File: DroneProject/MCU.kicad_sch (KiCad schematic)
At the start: 24 parts, among them U41 STM32F410RBT6, Y41 LFXTAL003151

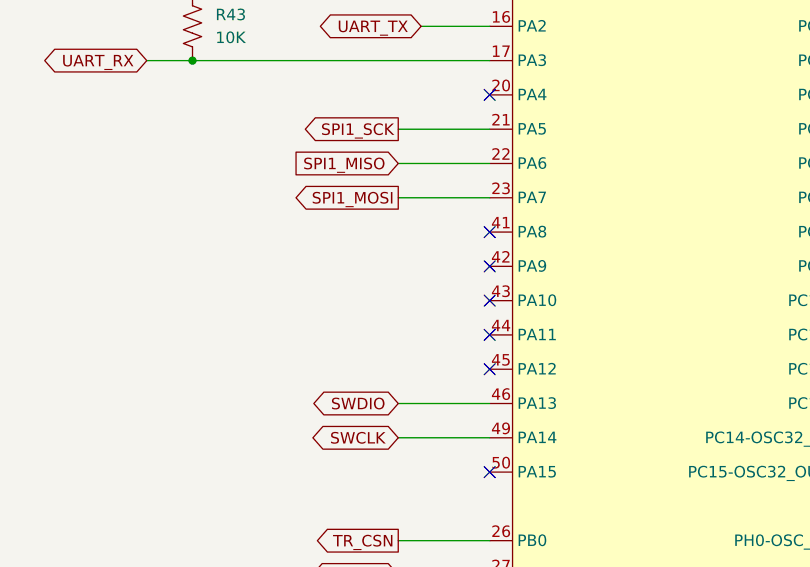
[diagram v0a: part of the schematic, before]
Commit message: Added mounting holes and some more testpoints.  Also started on PCB with dimesions and mounting holes measured and placed
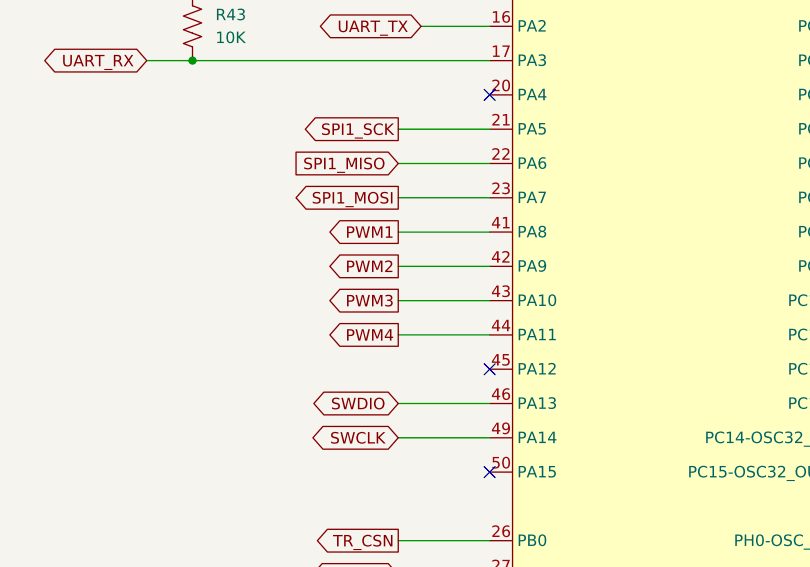
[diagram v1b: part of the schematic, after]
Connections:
- net PWM1: now reaches U41.41 (PA8)
- net PWM2: now reaches U41.42 (PA9)
- net PWM3: now reaches U41.43 (PA10)
- net PWM4: now reaches U41.44 (PA11)
- no-connect marks 23 -> 19
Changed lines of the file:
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@@
-	)
-	(no_connect
-		(at 68.58 71.12)
 	)
 	(no_connect
@@
 	)
 	(no_connect
-		(at 68.58 78.74)
-	)
-	(no_connect
 		(at 68.58 132.08)
 	)
 	(no_connect
-		(at 68.58 82.55)
-	)
-	(no_connect
 		(at 68.58 44.45)
 	)
@@
 	)
 	(no_connect
-		(at 68.58 74.93)
-	)
-	(no_connect
 		(at 109.22 52.07)
 	)
@@
 	(wire
 		(pts
+			(xy 58.42 71.12) (xy 68.58 71.12)
+		)
+		(stroke
+			(width 0)
+			(type default)
+		)
+	)
+	(wire
+		(pts
 			(xy 170.18 45.72) (xy 166.37 45.72)
 		)
@@
 	(wire
 		(pts
+			(xy 58.42 82.55) (xy 68.58 82.55)
+		)
+		(stroke
+			(width 0)
+			(type default)
+		)
+	)
+	(wire
+		(pts
 			(xy 166.37 45.72) (xy 166.37 48.26)
 		)
@@
 	(wire
 		(pts
+			(xy 58.42 74.93) (xy 68.58 74.93)
+		)
+		(stroke
+			(width 0)
+			(type default)
+		)
+	)
+	(wire
+		(pts
 			(xy 207.01 43.18) (xy 207.01 45.72)
 		)
@@
 		(pts
 			(xy 274.32 25.4) (xy 261.62 25.4)
+		)
+		(stroke
+			(width 0)
+			(type default)
+		)
+	)
+	(wire
+		(pts
+			(xy 58.42 78.74) (xy 68.58 78.74)
 		)
 		(stroke
@@
 		)
 	)
+	(global_label "PWM4"
+		(shape output)
+		(at 58.42 82.55 180)
+		(fields_autoplaced yes)
+		(effects
+			(font
+				(size 1.27 1.27)
+			)
+			(justify right)
+		)
+		(property "Intersheetrefs" "${INTERSHEET_REFS}"
+			(at 50.0525 82.55 0)
+			(effects
+				(font
+					(size 1.27 1.27)
+				)
+				(justify right)
+			)
+		)
+	)
 	(global_label "SPI1_MISO"
 		(shape input)
@@
 		)
 	)
+	(global_label "PWM1"
+		(shape output)
+		(at 58.42 71.12 180)
+		(fields_autoplaced yes)
+		(effects
+			(font
+				(size 1.27 1.27)
+			)
+			(justify right)
+		)
+		(property "Intersheetrefs" "${INTERSHEET_REFS}"
+			(at 50.0525 71.12 0)
+			(effects
+				(font
+					(size 1.27 1.27)
+				)
+				(justify right)
+			)
+		)
+	)
 	(global_label "SWCLK"
 		(shape bidirectional)
@@
 			)
 		)
+	)
+	(global_label "PWM3"
+		(shape output)
+		(at 58.42 78.74 180)
+		(fields_autoplaced yes)
+		(effects
+			(font
+				(size 1.27 1.27)
+			)
+			(justify right)
+		)
+		(property "Intersheetrefs" "${INTERSHEET_REFS}"
+			(at 50.0525 78.74 0)
+			(effects
+				(font
+					(size 1.27 1.27)
+				)
+				(justify right)
+			)
+		)
+	)
+	(global_label "PWM2"
+		(shape output)
+		(at 58.42 74.93 180)
+		(fields_autoplaced yes)
+		(effects
+			(font
+				(size 1.27 1.27)
+			)
+			(justify right)
+		)
+		(property "Intersheetrefs" "${INTERSHEET_REFS}"
+			(at 50.0525 74.93 0)
+			(effects
+				(font
+					(size 1.27 1.27)
+				)
+				(justify right)
+			)
+		)

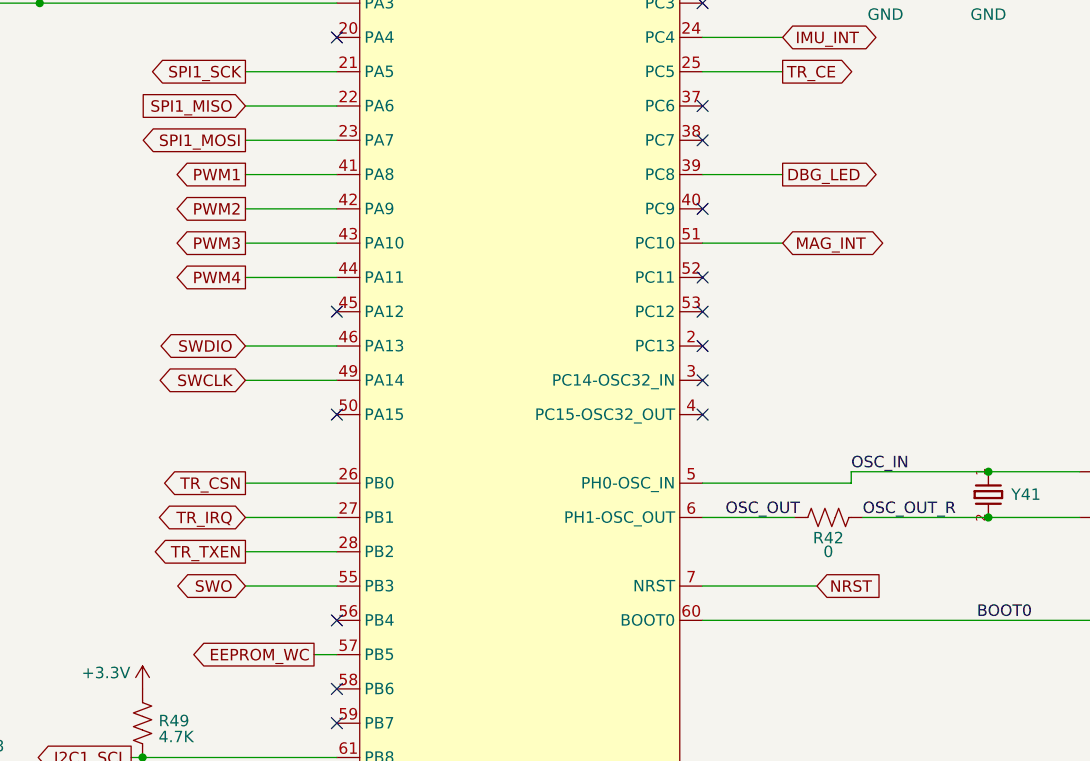
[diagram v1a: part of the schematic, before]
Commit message: Added a second MCU for motor control.  Removed 5V rail.  Added COM switching for SWD and UART external headers
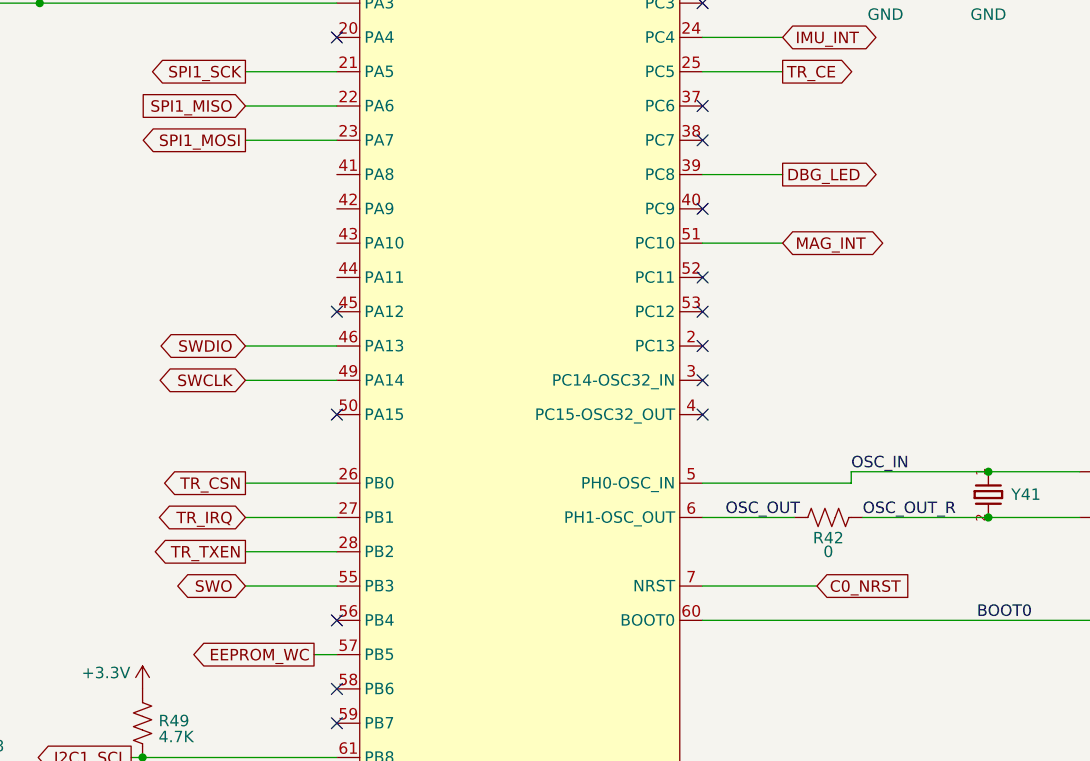
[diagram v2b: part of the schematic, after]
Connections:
- net NRST renamed C0_NRST
- net PWM1: no longer names the net of U41.41 (PA8)
- net PWM2: no longer names the net of U41.42 (PA9)
- net PWM3: no longer names the net of U41.43 (PA10)
- net PWM4: no longer names the net of U41.44 (PA11)
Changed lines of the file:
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@@
-	(wire
-		(pts
-			(xy 58.42 71.12) (xy 68.58 71.12)
-		)
-		(stroke
-			(width 0)
-			(type default)
-		)
-	)
 	(wire
 		(pts
@@
 	(wire
 		(pts
-			(xy 58.42 82.55) (xy 68.58 82.55)
-		)
-		(stroke
-			(width 0)
-			(type default)
-		)
-	)
-	(wire
-		(pts
 			(xy 166.37 45.72) (xy 166.37 48.26)
 		)
@@
 	(wire
 		(pts
-			(xy 58.42 74.93) (xy 68.58 74.93)
-		)
-		(stroke
-			(width 0)
-			(type default)
-		)
-	)
-	(wire
-		(pts
 			(xy 207.01 43.18) (xy 207.01 45.72)
 		)
@@
 		(pts
 			(xy 274.32 25.4) (xy 261.62 25.4)
-		)
-		(stroke
-			(width 0)
-			(type default)
-		)
-	)
-	(wire
-		(pts
-			(xy 58.42 78.74) (xy 68.58 78.74)
 		)
 		(stroke
@@
 		)
 	)
-	(global_label "PWM4"
-		(shape output)
-		(at 58.42 82.55 180)
-		(fields_autoplaced yes)
-		(effects
-			(font
-				(size 1.27 1.27)
-			)
-			(justify right)
-		)
-		(property "Intersheetrefs" "${INTERSHEET_REFS}"
-			(at 50.0525 82.55 0)
-			(effects
-				(font
-					(size 1.27 1.27)
-				)
-				(justify right)
-			)
-		)
-	)
 	(global_label "SPI1_MISO"
 		(shape input)
@@
 		)
 	)
-	(global_label "PWM1"
-		(shape output)
-		(at 58.42 71.12 180)
-		(fields_autoplaced yes)
-		(effects
-			(font
-				(size 1.27 1.27)
-			)
-			(justify right)
-		)
-		(property "Intersheetrefs" "${INTERSHEET_REFS}"
-			(at 50.0525 71.12 0)
-			(effects
-				(font
-					(size 1.27 1.27)
-				)
-				(justify right)
-			)
-		)
-	)
 	(global_label "SWCLK"
 		(shape bidirectional)
@@
 		)
 	)
-	(global_label "PWM3"
-		(shape output)
-		(at 58.42 78.74 180)
-		(fields_autoplaced yes)
-		(effects
-			(font
-				(size 1.27 1.27)
-			)
-			(justify right)
-		)
-		(property "Intersheetrefs" "${INTERSHEET_REFS}"
-			(at 50.0525 78.74 0)
-			(effects
-				(font
-					(size 1.27 1.27)
-				)
-				(justify right)
-			)
-		)
-	)
-	(global_label "PWM2"
-		(shape output)
-		(at 58.42 74.93 180)
-		(fields_autoplaced yes)
-		(effects
-			(font
-				(size 1.27 1.27)
-			)
-			(justify right)
-		)
-		(property "Intersheetrefs" "${INTERSHEET_REFS}"
-			(at 50.0525 74.93 0)
-			(effects
-				(font
-					(size 1.27 1.27)
-				)
-				(justify right)
-			)
-		)
-	)
 	(global_label "TR_TXEN"
 		(shape output)
@@
 		)
 	)
-	(global_label "NRST"
+	(global_label "C0_NRST"
 		(shape input)
 		(at 121.92 116.84 0)
@@
 		)
 		(property "Intersheetrefs" "${INTERSHEET_REFS}"
-			(at 129.6828 116.84 0)
-			(effects
-				(font
+			(at 133.1299 116.84 0)
+			(effects
+				(font

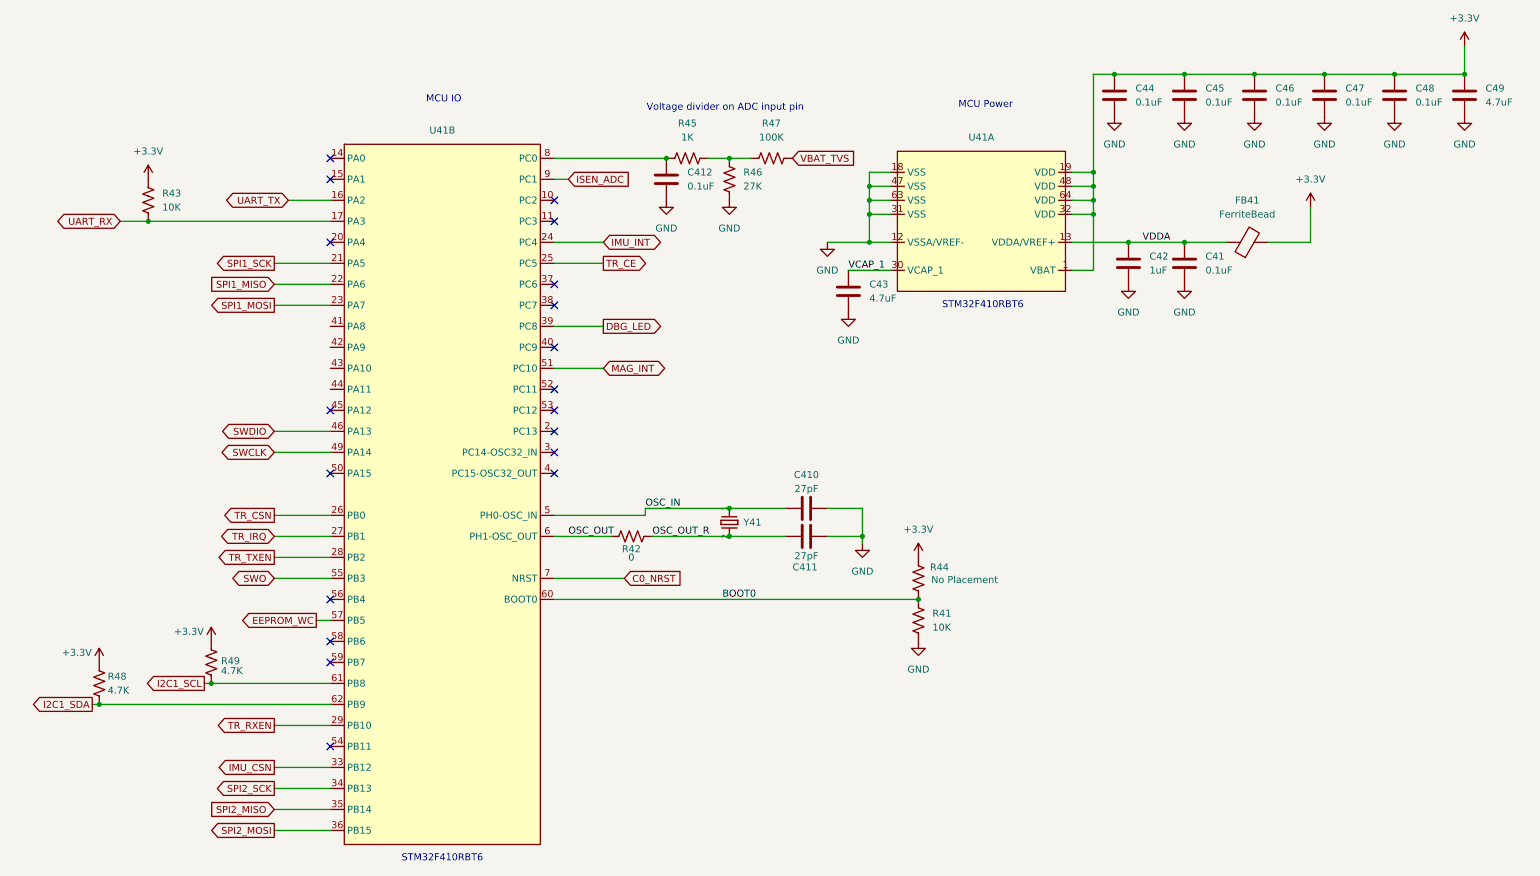
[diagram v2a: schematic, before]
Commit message: Changed motor controller to higher pin count MCU.  Defined all the pins for 3x PWM control over 4 motors.  Renamed a couple of global IO signals to indicate MCU origin (C0 vs C1)
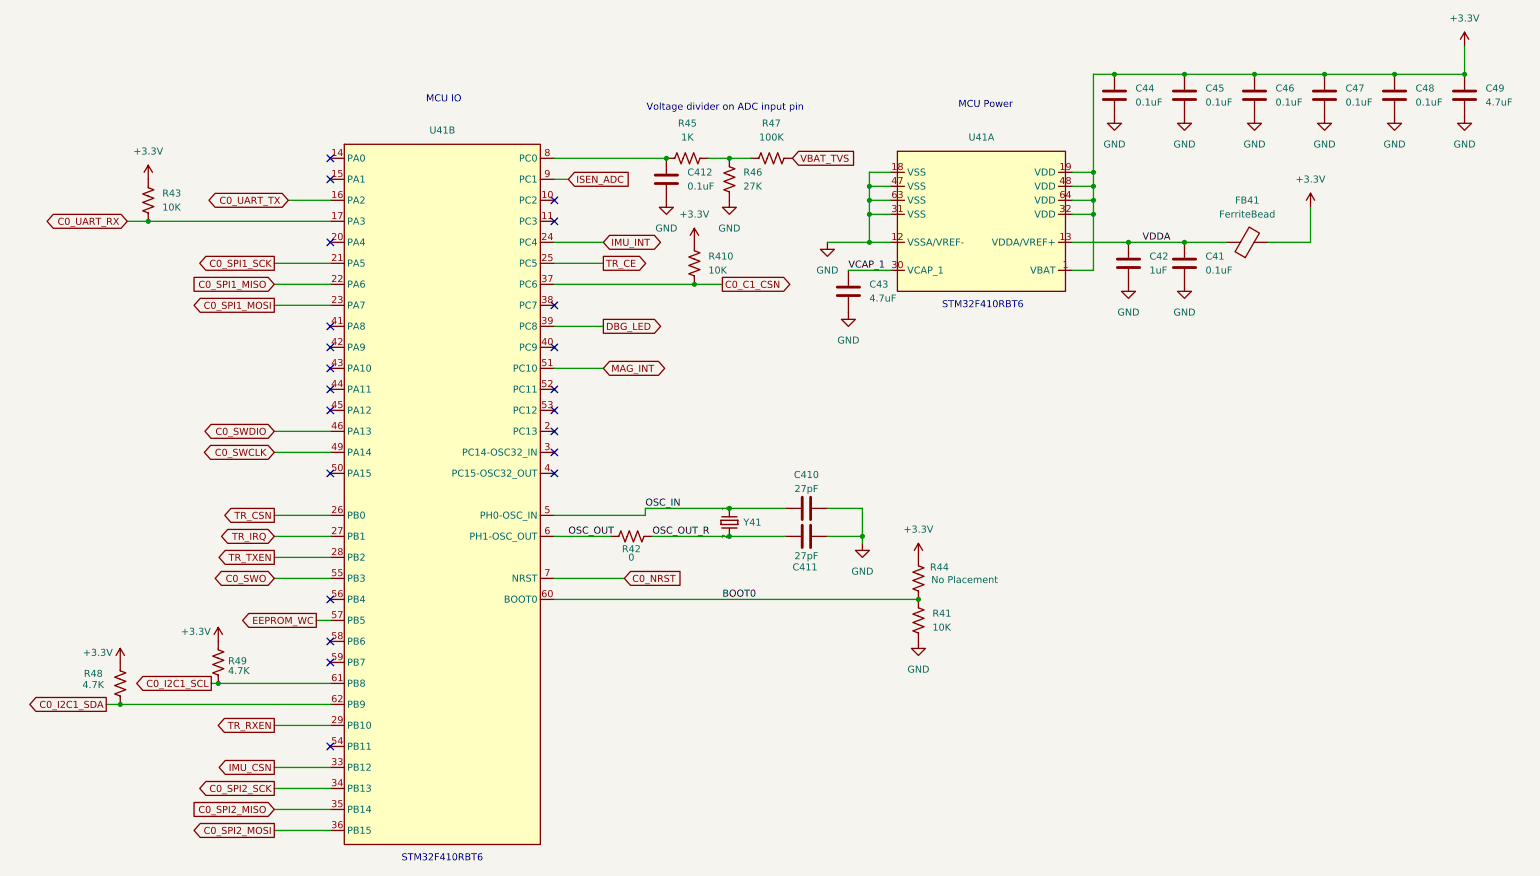
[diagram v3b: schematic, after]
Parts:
- added R410: 10K, Resistor_SMD:R_0402_1005Metric, symbol Device:R_US
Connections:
- net +3.3V: now also R410.2
- net C0_C1_CSN: now reaches U41.37 (PC6)
- net C0_C1_CSN: now also R410.1
- net I2C1_SCL renamed C0_I2C1_SCL
- net I2C1_SDA renamed C0_I2C1_SDA
- net SPI1_MISO renamed C0_SPI1_MISO
- net SPI1_MOSI renamed C0_SPI1_MOSI
- net SPI1_SCK renamed C0_SPI1_SCK
- net SPI2_MISO renamed C0_SPI2_MISO
- net SPI2_MOSI renamed C0_SPI2_MOSI
- net SPI2_SCK renamed C0_SPI2_SCK
- net SWCLK renamed C0_SWCLK
- net SWDIO renamed C0_SWDIO
- net SWO renamed C0_SWO
- net UART_RX renamed C0_UART_RX
- net UART_TX renamed C0_UART_TX
- no-connect marks 19 -> 22
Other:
- moved on the sheet: R48, R49

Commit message: Finished motor and C1 designs, still need to rename components on MTR2, 3, and 4 pages
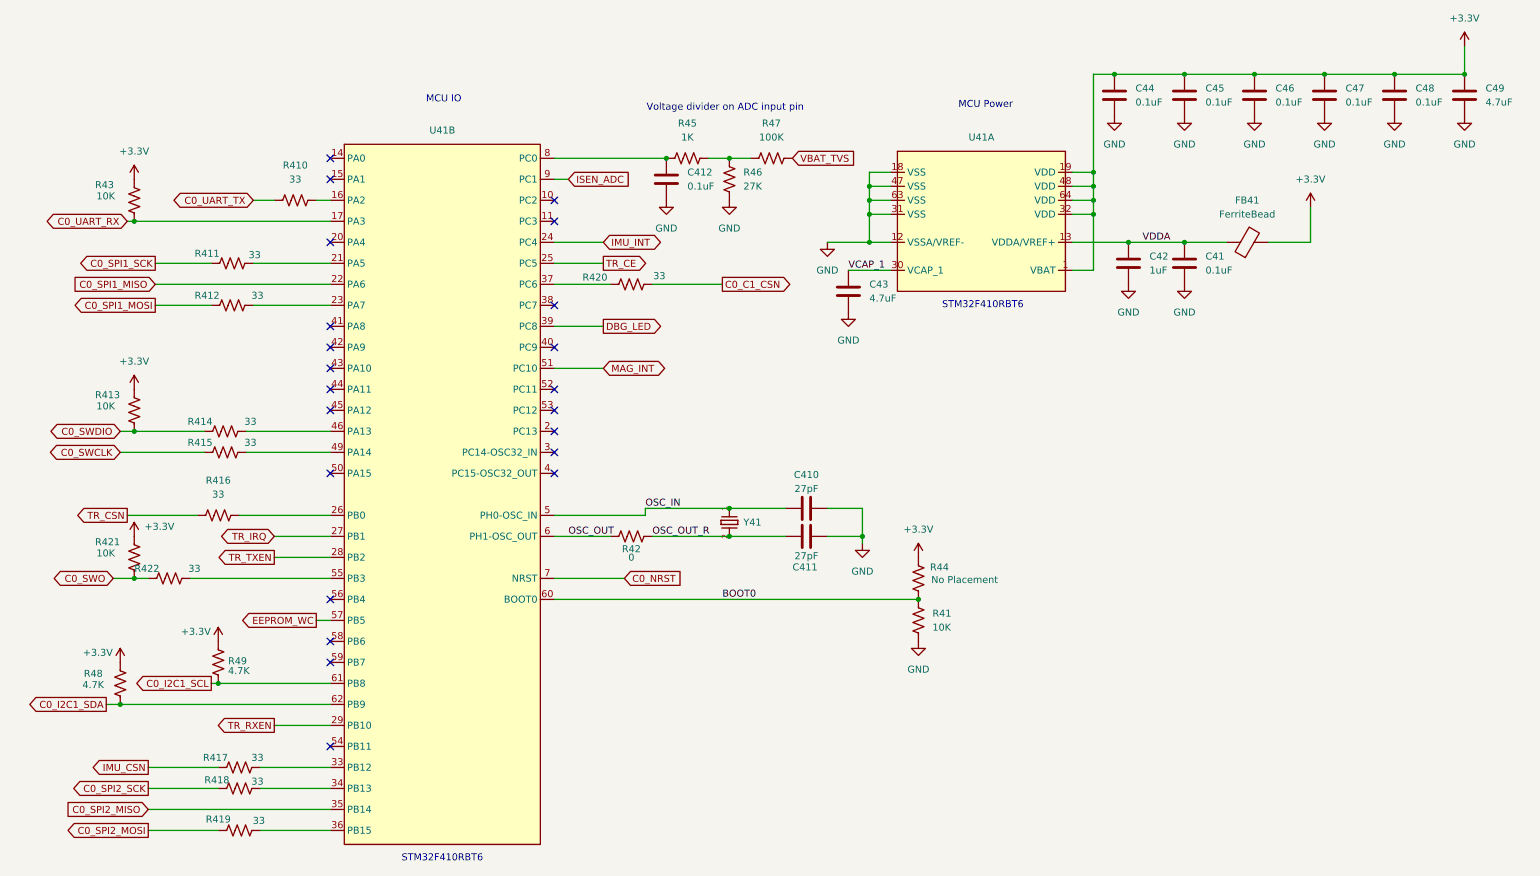
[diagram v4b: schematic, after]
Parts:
- added R411, R412, R414, R415, R416, R417, R418, R419, R420, R422: 33, Resistor_SMD:R_0402_1005Metric, symbol Device:R_US
- added R413, R421: 10K, Resistor_SMD:R_0402_1005Metric, symbol Device:R_US
- R410: value 10K -> 33
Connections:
- net +3.3V: now also R413.2, R421.2; no longer R410.2
- net C0_C1_CSN: now also R420.2; no longer R410.1, U41.37 (PC6)
- net C0_SPI1_MOSI: now also R412.1; no longer U41.23 (PA7)
- net C0_SPI1_SCK: now also R411.1; no longer U41.21 (PA5)
- net C0_SPI2_MOSI: now also R419.1; no longer U41.36 (PB15)
- net C0_SPI2_SCK: now also R418.1; no longer U41.34 (PB13)
- net C0_SWCLK: now also R415.1; no longer U41.49 (PA14)
- net C0_SWDIO: now also R413.1, R414.1; no longer U41.46 (PA13)
- net C0_SWO: now also R421.1, R422.1; no longer U41.55 (PB3)
- net C0_UART_TX: now also R410.1; no longer U41.16 (PA2)
- net IMU_CSN: now also R417.1; no longer U41.33 (PB12)
- net TR_CSN: now also R416.1; no longer U41.26 (PB0)
- new net: R417.2, U41.33 (PB12)
- new net: R418.2, U41.34 (PB13)
- new net: R411.2, U41.21 (PA5)
- new net: R420.1, U41.37 (PC6)
- new net: R410.2, U41.16 (PA2)
- new net: R419.2, U41.36 (PB15)
- new net: R412.2, U41.23 (PA7)
- new net: R416.2, U41.26 (PB0)
- new net: R414.2, U41.46 (PA13)
- new net: R415.2, U41.49 (PA14)
- new net: R422.2, U41.55 (PB3)
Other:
- moved on the sheet: R43
